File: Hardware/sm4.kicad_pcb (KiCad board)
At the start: 2 copper layers, 7 parts, among them Q1 NDT2955, U1 STM32F412RETx, U2 TMC2100-TA, U3 TMC2100-TA, U4 LM2594HVM-5.0, U5 MCP1700-3302E_SOT23

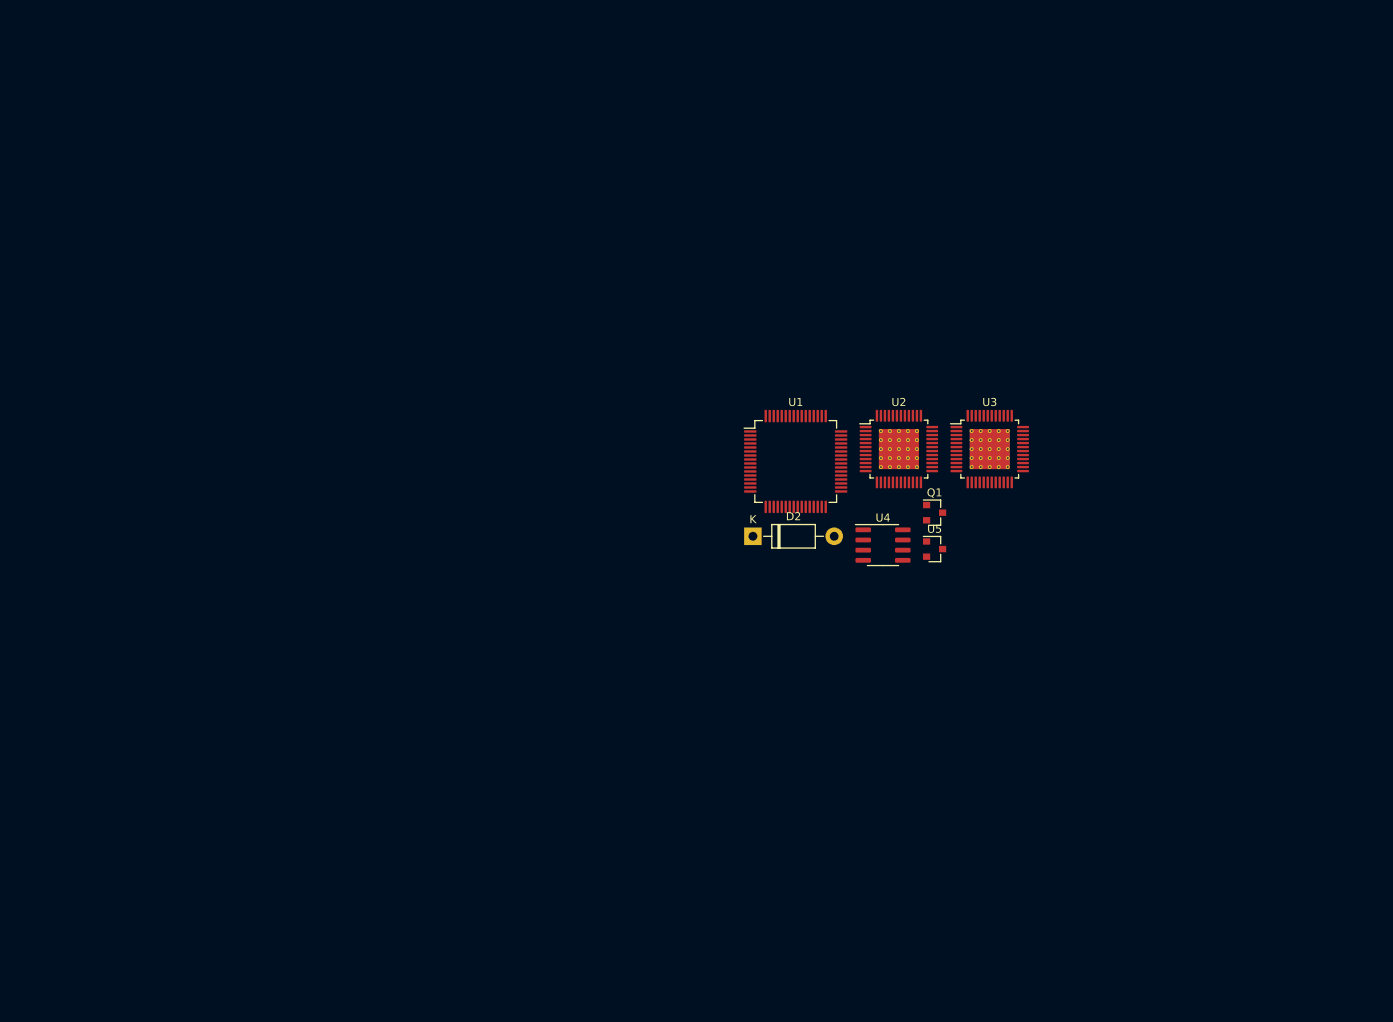
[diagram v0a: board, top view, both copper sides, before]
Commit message: Add packages to components.
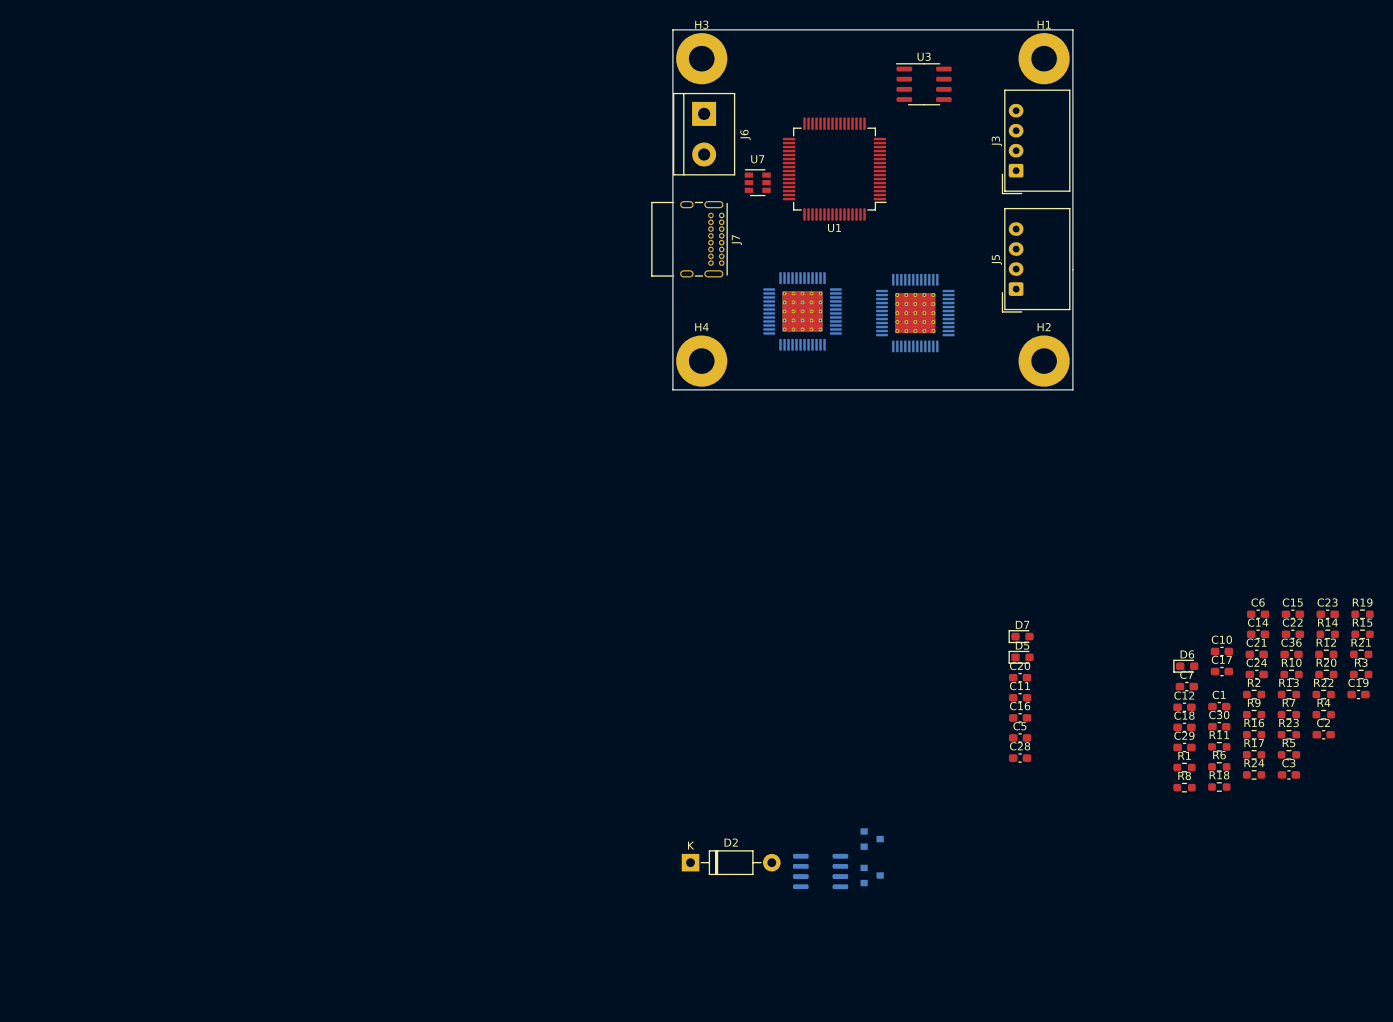
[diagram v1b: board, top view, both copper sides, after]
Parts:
- added C1: 2u2, Capacitor_SMD:C_0603_1608Metric_Pad1.08x0.95mm_HandSolder, F.Cu at (188.3, 134.6)
- added C10: 470n, Capacitor_SMD:C_0603_1608Metric_Pad1.08x0.95mm_HandSolder, F.Cu at (188.6, 127.7)
- added C11: 10n, Capacitor_SMD:C_0603_1608Metric_Pad1.08x0.95mm_HandSolder, F.Cu at (163.4, 133.5)
- added C12: 100n, Capacitor_SMD:C_0603_1608Metric_Pad1.08x0.95mm_HandSolder, F.Cu at (183.9, 134.7)
- added C14: 12p, Capacitor_SMD:C_0603_1608Metric_Pad1.08x0.95mm_HandSolder, F.Cu at (193.2, 125.6)
- added C15: 100n, Capacitor_SMD:C_0603_1608Metric_Pad1.08x0.95mm_HandSolder, F.Cu at (197.5, 123.0)
- added C16: 10n, Capacitor_SMD:C_0603_1608Metric_Pad1.08x0.95mm_HandSolder, F.Cu at (163.4, 136.0)
- added C17: 12p, Capacitor_SMD:C_0603_1608Metric_Pad1.08x0.95mm_HandSolder, F.Cu at (188.6, 130.2)
- added C18: 100n, Capacitor_SMD:C_0603_1608Metric_Pad1.08x0.95mm_HandSolder, F.Cu at (183.9, 137.2)
- added C19: 100n, Capacitor_SMD:C_0603_1608Metric_Pad1.08x0.95mm_HandSolder, F.Cu at (205.7, 133.1)
- added C2: 100n, Capacitor_SMD:C_0603_1608Metric_Pad1.08x0.95mm_HandSolder, F.Cu at (201.3, 138.1)
- added C20: 100n, Capacitor_SMD:C_0603_1608Metric_Pad1.08x0.95mm_HandSolder, F.Cu at (163.4, 131.0)
- added C21: 100n, Capacitor_SMD:C_0603_1608Metric_Pad1.08x0.95mm_HandSolder, F.Cu at (193.0, 128.1)
- added C22: 100n, Capacitor_SMD:C_0603_1608Metric_Pad1.08x0.95mm_HandSolder, F.Cu at (197.5, 125.6)
- added C23: 100n, Capacitor_SMD:C_0603_1608Metric_Pad1.08x0.95mm_HandSolder, F.Cu at (201.8, 123.0)
- added C24: 100n, Capacitor_SMD:C_0603_1608Metric_Pad1.08x0.95mm_HandSolder, F.Cu at (193.0, 130.6)
- added C28: 100n, Capacitor_SMD:C_0603_1608Metric_Pad1.08x0.95mm_HandSolder, F.Cu at (163.4, 141.0)
- added C29: 100n, Capacitor_SMD:C_0603_1608Metric_Pad1.08x0.95mm_HandSolder, F.Cu at (183.9, 139.7)
- added C3: 100n, Capacitor_SMD:C_0603_1608Metric_Pad1.08x0.95mm_HandSolder, F.Cu at (197.0, 143.1)
- added C30: 470n, Capacitor_SMD:C_0603_1608Metric_Pad1.08x0.95mm_HandSolder, F.Cu at (188.3, 137.1)
- added C36: 10n, Capacitor_SMD:C_0603_1608Metric_Pad1.08x0.95mm_HandSolder, F.Cu at (197.3, 128.1)
- added C5: 100n, Capacitor_SMD:C_0603_1608Metric_Pad1.08x0.95mm_HandSolder, F.Cu at (163.4, 138.5)
- added C6: 100n, Capacitor_SMD:C_0603_1608Metric_Pad1.08x0.95mm_HandSolder, F.Cu at (193.2, 123.0)
- added C7: 470n, Capacitor_SMD:C_0603_1608Metric_Pad1.08x0.95mm_HandSolder, F.Cu at (184.2, 132.1)
- added D5: LED_Small, LED_SMD:LED_0603_1608Metric_Pad1.05x0.95mm_HandSolder, F.Cu at (163.7, 128.4)
- added D6: LED_Small, LED_SMD:LED_0603_1608Metric_Pad1.05x0.95mm_HandSolder, F.Cu at (184.3, 129.5)
- added D7: LED_Small, LED_SMD:LED_0603_1608Metric_Pad1.05x0.95mm_HandSolder, F.Cu at (163.7, 125.8)
- added H1: MountingHole_Pad, MountingHole:MountingHole_3.2mm_M3_Pad, F.Cu at (166.4, 53.6)
- added H2: MountingHole_Pad, MountingHole:MountingHole_3.2mm_M3_Pad, F.Cu at (166.4, 91.4)
- added H3: MountingHole_Pad, MountingHole:MountingHole_3.2mm_M3_Pad, F.Cu at (123.6, 53.6)
- added H4: MountingHole_Pad, MountingHole:MountingHole_3.2mm_M3_Pad, F.Cu at (123.6, 91.4)
- added J3: CAN bus, Connector_Molex:Molex_SPOX_5268-04A_1x04_P2.50mm_Horizontal, F.Cu at (162.9, 67.6)
- added J5: I2C, Connector_Molex:Molex_SPOX_5268-04A_1x04_P2.50mm_Horizontal, F.Cu at (162.9, 82.4)
- added J6: Power, TerminalBlock:TerminalBlock_bornier-2_P5.08mm, F.Cu at (123.9, 60.5)
- added J7: USB_C_Receptacle_USB2.0, Connector_USB:USB_C_Receptacle_GCT_USB4085, F.Cu at (126.1, 73.2)
- added R1: 10k, Resistor_SMD:R_0603_1608Metric_Pad0.98x0.95mm_HandSolder, F.Cu at (183.9, 142.2)
- added R10: 1M, Resistor_SMD:R_0603_1608Metric_Pad0.98x0.95mm_HandSolder, F.Cu at (197.3, 130.6)
- added R11: 0R, Resistor_SMD:R_0603_1608Metric_Pad0.98x0.95mm_HandSolder, F.Cu at (188.3, 139.6)
- added R12: 47R9, Resistor_SMD:R_0603_1608Metric_Pad0.98x0.95mm_HandSolder, F.Cu at (201.7, 128.1)
- added R13: 47R9, Resistor_SMD:R_0603_1608Metric_Pad0.98x0.95mm_HandSolder, F.Cu at (197.0, 133.1)
- added R14: 10k, Resistor_SMD:R_0603_1608Metric_Pad0.98x0.95mm_HandSolder, F.Cu at (201.8, 125.6)
- added R15: 2R2, Resistor_SMD:R_0603_1608Metric_Pad0.98x0.95mm_HandSolder, F.Cu at (206.2, 125.6)
- added R16: 1R, Resistor_SMD:R_0603_1608Metric_Pad0.98x0.95mm_HandSolder, F.Cu at (192.7, 138.1)
- added R17: 1R, Resistor_SMD:R_0603_1608Metric_Pad0.98x0.95mm_HandSolder, F.Cu at (192.7, 140.6)
- added R18: 100k, Resistor_SMD:R_0603_1608Metric_Pad0.98x0.95mm_HandSolder, F.Cu at (188.3, 144.6)
- added R19: 4k7, Resistor_SMD:R_0603_1608Metric_Pad0.98x0.95mm_HandSolder, F.Cu at (206.2, 123.0)
- added R2: 2R2, Resistor_SMD:R_0603_1608Metric_Pad0.98x0.95mm_HandSolder, F.Cu at (192.7, 133.1)
- added R20: 1k, Resistor_SMD:R_0603_1608Metric_Pad0.98x0.95mm_HandSolder, F.Cu at (201.7, 130.6)
- added R21: 1k, Resistor_SMD:R_0603_1608Metric_Pad0.98x0.95mm_HandSolder, F.Cu at (206.0, 128.1)
- added R22: 5k1, Resistor_SMD:R_0603_1608Metric_Pad0.98x0.95mm_HandSolder, F.Cu at (201.3, 133.1)
- added R23: 5k1, Resistor_SMD:R_0603_1608Metric_Pad0.98x0.95mm_HandSolder, F.Cu at (197.0, 138.1)
- added R24: 1k, Resistor_SMD:R_0603_1608Metric_Pad0.98x0.95mm_HandSolder, F.Cu at (192.7, 143.1)
- added R3: 1R, Resistor_SMD:R_0603_1608Metric_Pad0.98x0.95mm_HandSolder, F.Cu at (206.0, 130.6)
- added R4: 10k, Resistor_SMD:R_0603_1608Metric_Pad0.98x0.95mm_HandSolder, F.Cu at (201.3, 135.6)
- added R5: 1R, Resistor_SMD:R_0603_1608Metric_Pad0.98x0.95mm_HandSolder, F.Cu at (197.0, 140.6)
- added R6: 47R, Resistor_SMD:R_0603_1608Metric_Pad0.98x0.95mm_HandSolder, F.Cu at (188.3, 142.1)
- added R7: 0R, Resistor_SMD:R_0603_1608Metric_Pad0.98x0.95mm_HandSolder, F.Cu at (197.0, 135.6)
- added R8: 1M, Resistor_SMD:R_0603_1608Metric_Pad0.98x0.95mm_HandSolder, F.Cu at (183.9, 144.7)
- added R9: 10k, Resistor_SMD:R_0603_1608Metric_Pad0.98x0.95mm_HandSolder, F.Cu at (192.7, 135.6)
- added U6: MCP1700-3302E_SOT23, Package_TO_SOT_SMD:SOT-23, B.Cu at (144.9, 155.7)
- added U7: USBLC6-2SC6, Package_TO_SOT_SMD:SOT-23-6, F.Cu at (130.6, 69.1)
- Q1, U2: moved to B.Cu
- U3: value TMC2100-TA -> MCP2562-E-SN; footprint Package_QFP:TQFP-48-1EP_7x7mm_P0.5mm_EP5x5mm_ThermalVias -> Package_SO:SOIC-8_3.9x4.9mm_P1.27mm
- U4: value LM2594HVM-5.0 -> TMC2100-TA; footprint Package_SO:SOIC-8_3.9x4.9mm_P1.27mm -> Package_QFP:TQFP-48-1EP_7x7mm_P0.5mm_EP5x5mm_ThermalVias; moved to B.Cu
- U5: value MCP1700-3302E_SOT23 -> LM2594HVM-5.0; footprint Package_TO_SOT_SMD:SOT-23 -> Package_SO:SOIC-8_3.9x4.9mm_P1.27mm; moved to B.Cu
- moved U3 46.3 mm to (151.4, 56.8)
- moved U5 42.7 mm to (138.5, 155.2)
- moved Q1 41.5 mm to (144.9, 151.2)
- moved D2 41.5 mm to (122.2, 154.1)
- moved U1 36.9 mm to (140.2, 67.4), turned to 180 degrees
- moved U4 29.3 mm to (150.3, 85.4)
- moved U2 21.0 mm to (136.2, 85.2)
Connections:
- Q1 pad 1: (no net) -> Net-(D1-Pad2)
- Q1 pad 3: (no net) -> VS1
- U1 pad 13: (no net) -> VDDA
- U1 pad 30: (no net) -> Net-(C1-Pad1)
- U1 pad 44: (no net) -> USB_D-
- U1 pad 45: (no net) -> USB_D+
- U1 pad 5: (no net) -> OSC_IN
- U1 pad 6: (no net) -> OSC_OUT
- U1 pad 60: (no net) -> BOOT
- U1 pad 7: (no net) -> NRST
- U2 pad 1: (no net) -> GND
- U2 pad 10: (no net) -> +3V3
- U2 pad 12: Net-(U2-Pad12) -> GND
- U2 pad 13: Net-(U2-Pad13) -> GND
- U2 pad 17: (no net) -> Net-(R3-Pad2)
- U2 pad 2: (no net) -> GND
- U2 pad 21: (no net) -> VS1
- U2 pad 26: (no net) -> ERR1
- U2 pad 31: Net-(U2-Pad12) -> GND
- U2 pad 32: (no net) -> GND
- U2 pad 33: (no net) -> 5VOUT1
- U2 pad 34: (no net) -> 5VM1
- U2 pad 36: Net-(U2-Pad12) -> GND
- U2 pad 38: (no net) -> VCP1
- U2 pad 39: (no net) -> VSA1
- U2 pad 40: (no net) -> VS1
- U2 pad 44: (no net) -> Net-(R5-Pad2)
- U2 pad 48: Net-(U2-Pad13) -> GND
- U2 pad 49: Net-(U2-Pad12) -> GND
- U2 pad 6: Net-(U2-Pad12) -> GND
- U3 pad 2: (no net) -> GND
- U3 pad 3: (no net) -> +5V
- U3 pad 5: (no net) -> Net-(R7-Pad2)
- U3 pad 6: Net-(U3-Pad12) -> Net-(J3-Pad2)
- U3 pad 7: (no net) -> Net-(J3-Pad3)
- U3 pad 8: (no net) -> Net-(R10-Pad2)
- U4 pad 1: (no net) -> GND
- U4 pad 2: (no net) -> GND
- U4 pad 5: GND -> (no net)
- U4 pad 8: Net-(D2-Pad1) -> (no net)
- U5 pad 2: +3V3 -> (no net)
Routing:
- added copper zone on In2.Cu, net +3V3
- added copper zone on In1.Cu, net GND
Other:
- board outline added: 50 x 45 mm
- copper layers 2 -> 4

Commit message: Finish first version of the PCB, which is trash and shall perish.
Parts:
- removed D2: 1N5817, Diode_THT:D_DO-41_SOD81_P10.16mm_Horizontal
- removed U5: LM2594HVM-5.0, Package_SO:SOIC-8_3.9x4.9mm_P1.27mm
- added C13: 1u, Capacitor_SMD:C_0603_1608Metric_Pad1.08x0.95mm_HandSolder, F.Cu at (151.6, 59.2)
- added C25: 1u, Capacitor_SMD:C_1206_3216Metric_Pad1.33x1.80mm_HandSolder, B.Cu at (164.2, 54.8)
- added C26: 47u, Capacitor_SMD:C_Elec_8x6.2, B.Cu at (153.3, 94.8)
- added C27: 68u, Capacitor_SMD:C_Elec_6.3x7.7, B.Cu at (156.9, 58.5)
- added C31: 22n@50V, Capacitor_SMD:C_0603_1608Metric_Pad1.08x0.95mm_HandSolder, B.Cu at (161.7, 88.5)
- added C32: 470n, Capacitor_SMD:C_0603_1608Metric_Pad1.08x0.95mm_HandSolder, B.Cu at (162.6, 91.3)
- added C34: 1u, Capacitor_SMD:C_0603_1608Metric_Pad1.08x0.95mm_HandSolder, B.Cu at (128.6, 53.5)
- added C35: 1u, Capacitor_SMD:C_0603_1608Metric_Pad1.08x0.95mm_HandSolder, B.Cu at (135.4, 53.4)
- added C4: 47u, Capacitor_SMD:C_Elec_8x6.2, B.Cu at (125.5, 88.2)
- added C8: 4u7, Capacitor_SMD:C_0603_1608Metric_Pad1.08x0.95mm_HandSolder, B.Cu at (135.6, 68.3)
- added C9: 22n@50V, Capacitor_SMD:C_0603_1608Metric_Pad1.08x0.95mm_HandSolder, B.Cu at (136.2, 88.3)
- added D1: 4V7, Diode_SMD:D_SOD-123, B.Cu at (172.1, 54.0)
- added D3: D_Small, Diode_SMD:D_SOD-123, B.Cu at (162.7, 58.6)
- added D4: D_Small, Diode_SMD:D_SOD-123, F.Cu at (129.7, 57.4)
- added F1: 500mA, Fuse:Fuse_1206_3216Metric_Pad1.42x1.75mm_HandSolder, B.Cu at (168.1, 52.4)
- added F2: 500mA, Fuse:Fuse_1206_3216Metric_Pad1.42x1.75mm_HandSolder, F.Cu at (129.8, 60.1)
- added FB1: 1k @ 100 MHz, Resistor_SMD:R_0603_1608Metric_Pad0.98x0.95mm_HandSolder, F.Cu at (149.9, 59.2)
- added FB2: 1k @ 100 MHz, Resistor_SMD:R_0603_1608Metric_Pad0.98x0.95mm_HandSolder, B.Cu at (163.5, 52.3)
- added J1: Motor1, Connector_PinHeader_2.54mm:PinHeader_1x04_P2.54mm_Horizontal, F.Cu at (145.3, 95.9)
- added J2: Termination, Connector_PinHeader_2.54mm:PinHeader_1x02_P2.54mm_Vertical, F.Cu at (173.9, 65.5)
- added J4: Motor2, Connector_PinHeader_2.54mm:PinHeader_1x04_P2.54mm_Horizontal, F.Cu at (168.5, 95.8)
- added J8: Conn_01x05_Male, Connector_Molex:Molex_SPOX_5267-05A_1x05_P2.50mm_Vertical, F.Cu at (131.8, 78.2)
- added SW1: RST_SW, Connector_PinHeader_2.54mm:PinHeader_1x02_P2.54mm_Vertical, F.Cu at (124.5, 71.5)
- added SW2: BOOT_SW, Button_Switch_SMD:SW_SPDT_PCM12, F.Cu at (152.4, 53.8)
- added Y1: 25 MHz, Crystal:Crystal_SMD_3225-4Pin_3.2x2.5mm_HandSoldering, F.Cu at (153.8, 65.3)
- C10, C11, C18, C30, C7, J7, R1, R14, R15, R16, R17, R2, R22, R3, R4, R5, R9: moved to B.Cu
- C2, C23, C24, C28, C29, C3, C5, C6: footprint Capacitor_SMD:C_0603_1608Metric_Pad1.08x0.95mm_HandSolder -> Capacitor_SMD:C_0805_2012Metric_Pad1.18x1.45mm_HandSolder; moved to B.Cu
- moved R23 106.3 mm to (122.6, 62.1)
- moved U6 103.0 mm to (131.5, 53.5), turned to 270 degrees
- moved Q1 102.4 mm to (175.4, 53.4)
- moved R22 98.9 mm to (128.0, 66.7), turned to 90 degrees
- moved C1 95.0 mm to (139.0, 53.4), turned to 90 degrees
- moved C12 93.8 mm to (137.2, 53.4), turned to 90 degrees
- moved R4 91.4 mm to (143.4, 64.9), turned to 270 degrees
- moved R6 88.5 mm to (150.8, 62.0)
- moved C19 86.3 mm to (149.1, 67.9)
- moved C15 86.2 mm to (145.4, 54.3)
- moved R5 85.8 mm to (134.5, 81.8)
- moved C3 85.5 mm to (132.8, 86.6)
- moved C18 85.1 mm to (133.9, 68.3), turned to 270 degrees
- moved C2 84.4 mm to (132.8, 88.9)
- moved R11 83.9 mm to (167.1, 58.5), turned to 90 degrees
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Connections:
- J3 pad 4: +5V -> VDC
- J5 pad 2: (no net) -> SCL
- J5 pad 3: (no net) -> SDA
- J5 pad 4: +5V -> VDC
- Q1 pad 2: (no net) -> Net-(D1-Pad1)
- Q1 pad 3: VS1 -> VDC
- R12 pad 1: (no net) -> Net-(J2-Pad2)
- R13 pad 1: (no net) -> Net-(J2-Pad1)
- R21 pad 2: (no net) -> STATUS
- R24 pad 2: (no net) -> ERR
- R4 pad 1: (no net) -> Net-(R4-Pad1)
- U1 pad 10: (no net) -> CFG02
- U1 pad 11: (no net) -> DIR2
- U1 pad 14: (no net) -> VBAT
- U1 pad 15: (no net) -> CFG52
- U1 pad 16: (no net) -> CFG42
- U1 pad 2: (no net) -> STATUS
- U1 pad 3: (no net) -> ERR
- U1 pad 4: (no net) -> CFG32
- U1 pad 40: (no net) -> SDA
- U1 pad 41: (no net) -> SCL
- U1 pad 42: (no net) -> CFG41
- U1 pad 43: (no net) -> CFG51
- U1 pad 46: (no net) -> SWDIO
- U1 pad 49: (no net) -> SWCLK
- U1 pad 51: (no net) -> CFG31
- U1 pad 52: (no net) -> CFG21
- U1 pad 53: (no net) -> CFG11
- U1 pad 55: (no net) -> CFG01
- U1 pad 56: (no net) -> STEP1
- U1 pad 57: (no net) -> DIR1
- U1 pad 58: (no net) -> STEP2
- U1 pad 59: (no net) -> ERR1
- U1 pad 61: (no net) -> CAN_RX
- U1 pad 62: (no net) -> CAN_TX
- U1 pad 8: (no net) -> CFG22
- U1 pad 9: (no net) -> CFG12
- U2 pad 15: (no net) -> Net-(J1-Pad1)
- U2 pad 19: (no net) -> Net-(J1-Pad2)
- U2 pad 24: (no net) -> CFG41
- U2 pad 25: (no net) -> CFG51
- U2 pad 3: (no net) -> CFG31
- U2 pad 35: (no net) -> Net-(C9-Pad2)
- U2 pad 37: (no net) -> Net-(C9-Pad1)
- U2 pad 4: (no net) -> CFG21
- U2 pad 42: (no net) -> Net-(J1-Pad3)
- U2 pad 46: (no net) -> Net-(J1-Pad4)
- U2 pad 5: (no net) -> CFG11
- U2 pad 7: (no net) -> CFG01
- U2 pad 8: (no net) -> STEP1
- U2 pad 9: (no net) -> DIR1
- U3 pad 1: (no net) -> CAN_TX
- U3 pad 4: (no net) -> CAN_RX
- U4 pad 15: (no net) -> Net-(J4-Pad1)
- U4 pad 19: (no net) -> Net-(J4-Pad2)
- U4 pad 24: (no net) -> CFG42
- U4 pad 25: (no net) -> CFG52
- U4 pad 3: (no net) -> CFG32
- U4 pad 35: (no net) -> Net-(C31-Pad2)
- U4 pad 37: (no net) -> Net-(C31-Pad1)
- U4 pad 4: (no net) -> CFG22
- U4 pad 42: (no net) -> Net-(J4-Pad3)
- U4 pad 46: (no net) -> Net-(J4-Pad4)
- U4 pad 5: (no net) -> CFG12
- U4 pad 7: (no net) -> CFG02
- U4 pad 8: (no net) -> STEP2
- U4 pad 9: (no net) -> DIR2
- U6 pad 1: (no net) -> GND
- U7 pad 5: (no net) -> +5VD
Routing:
- net VS1: track 0.00 -> 111.1 mm, vias 0 -> 6
- net GND: track 0.00 -> 110.9 mm, vias 0 -> 78
- net SCL: track 0.00 -> 58.5 mm, vias 0 -> 1
- net SDA: track 0.00 -> 57.4 mm, vias 0 -> 1
- net +5V: track 0.00 -> 56.3 mm, vias 0 -> 3
- net NRST: track 0.00 -> 47.1 mm, vias 0 -> 1
- net CFG42: track 0.00 -> 43.5 mm, vias 0 -> 3
- net CFG52: track 0.00 -> 37.9 mm, vias 0 -> 3
- net DIR2: track 0.00 -> 35.8 mm, vias 0 -> 1
- net CFG02: track 0.00 -> 35.5 mm, vias 0 -> 3
- net CFG12: track 0.00 -> 33.5 mm, vias 0 -> 3
- net CFG22: track 0.00 -> 31.9 mm, vias 0 -> 3
- net Net-(J1-Pad4): track 0.00 -> 31.8 mm
- net STEP2: track 0.00 -> 31.7 mm, vias 0 -> 1
- net Net-(J1-Pad3): track 0.00 -> 31.5 mm
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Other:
- board size 50 x 45 mm -> 65 x 50 mm
